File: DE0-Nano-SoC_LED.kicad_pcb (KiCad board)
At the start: 2 copper layers, 96 x 178.3 mm, 23 parts, among them J1 Conn_02x08_Odd_Even, J10 Conn_01x01, J11 Conn_01x01, J12 Conn_01x01, J13 Conn_01x01, J14 Conn_01x01, J15 Conn_01x01, J16 Conn_01x10, J17 Conn_01x08, J18 Conn_01x06, J19 Conn_01x08, J2 Conn_02x08_Odd_Even, J3 Conn_02x20_Odd_Even, J4 Conn_02x20_Odd_Even, J5 Conn_02x08_Odd_Even, J6 Conn_02x08_Odd_Even, J7 Conn_02x08_Odd_Even, J8 Conn_01x01, J9 Conn_01x01, U1 74HC245, U2 74HC245

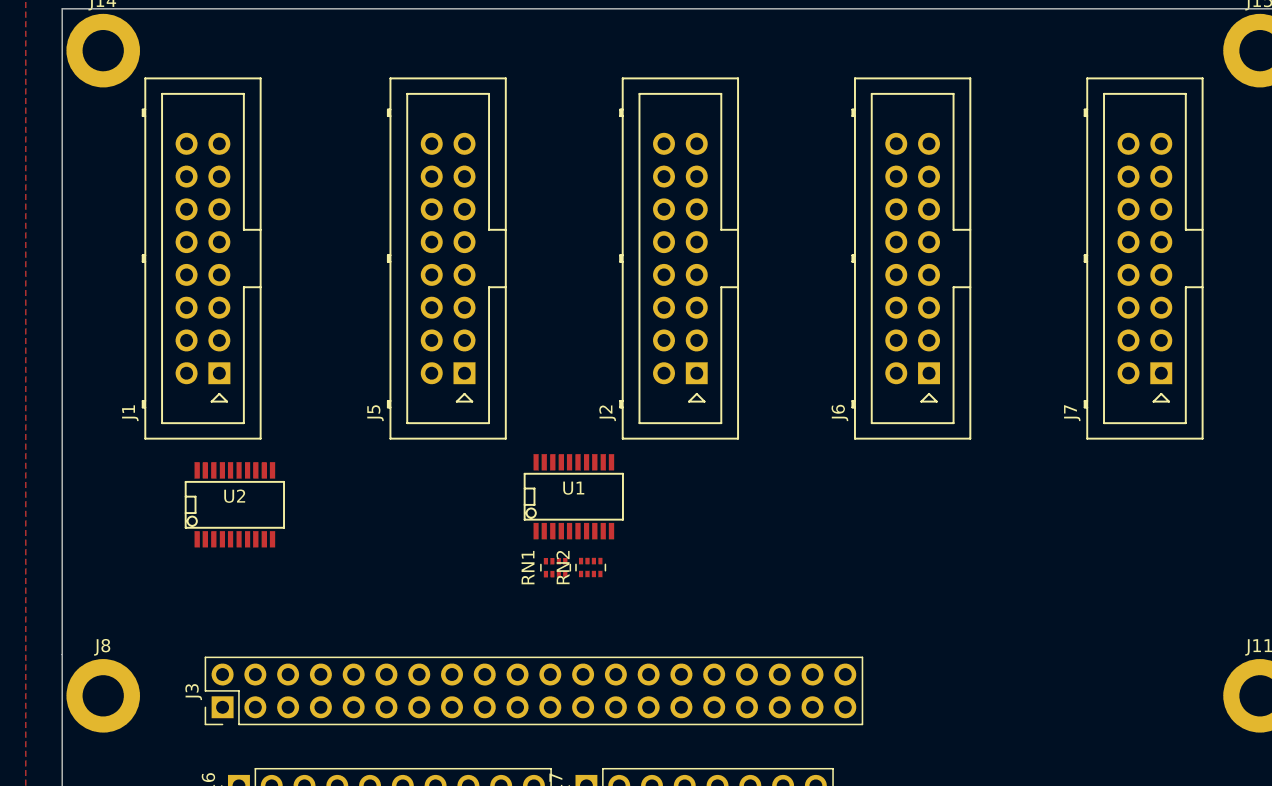
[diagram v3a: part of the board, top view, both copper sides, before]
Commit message: half of the components are almost placed
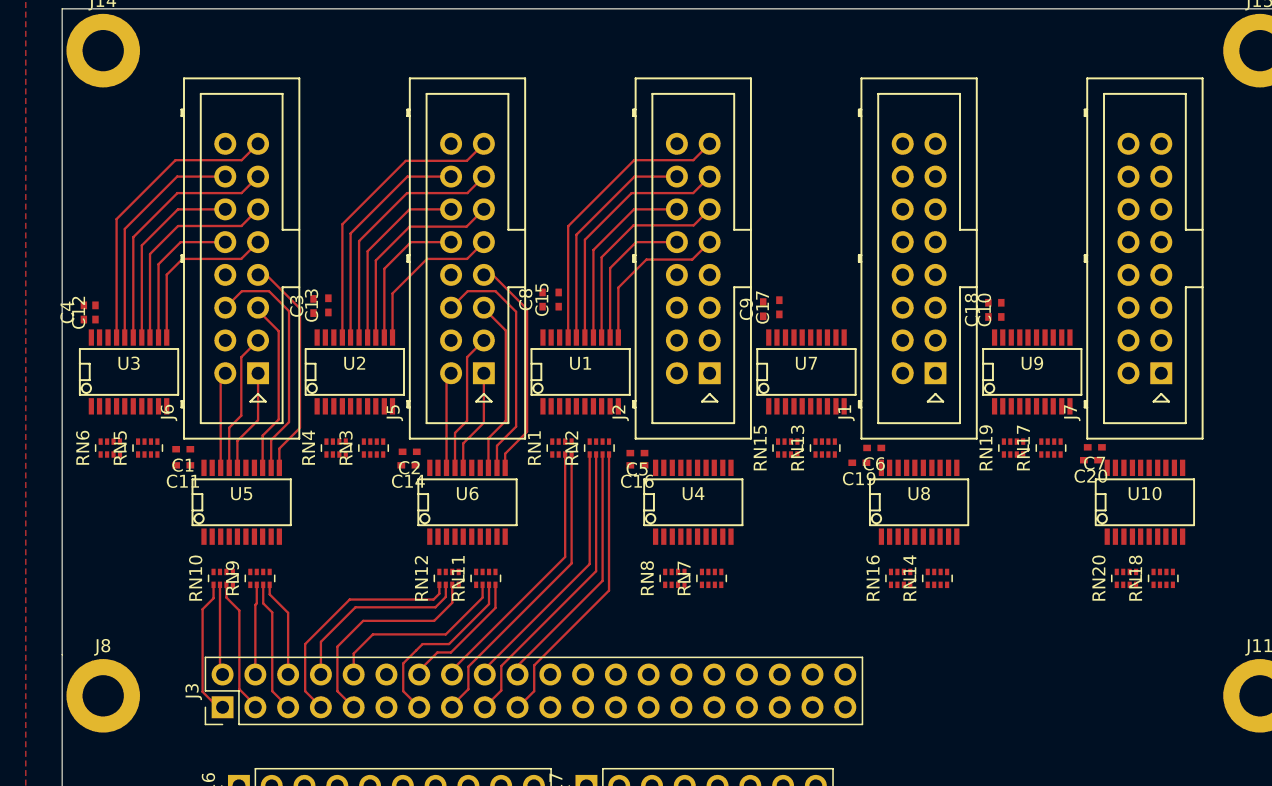
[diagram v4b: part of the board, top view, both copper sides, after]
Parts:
- added C1: 0.1, Capacitors_SMD:C_0402_NoSilk, F.Cu at (76.2, 50.9)
- added C10: 0.1, Capacitors_SMD:C_0402_NoSilk, F.Cu at (139.6, 40.1)
- added C11: 0.01, Capacitors_SMD:C_0402_NoSilk, F.Cu at (76.2, 52.1)
- added C12: 0.01, Capacitors_SMD:C_0402_NoSilk, F.Cu at (69.4, 40.3)
- added C13: 0.01, Capacitors_SMD:C_0402_NoSilk, F.Cu at (87.5, 39.7)
- added C14: 0.01, Capacitors_SMD:C_0402_NoSilk, F.Cu at (93.7, 52.1)
- added C15: 0.01, Capacitors_SMD:C_0402_NoSilk, F.Cu at (105.3, 39.3)
- added C16: 0.01, Capacitors_SMD:C_0402_NoSilk, F.Cu at (111.4, 52.1)
- added C17: 0.01, Capacitors_SMD:C_0402_NoSilk, F.Cu at (122.4, 39.9)
- added C18: 0.01, Capacitors_SMD:C_0402_NoSilk, F.Cu at (138.6, 40.1)
- added C19: 0.01, Capacitors_SMD:C_0402_NoSilk, F.Cu at (128.6, 51.9)
- added C2: 0.1, Capacitors_SMD:C_0402_NoSilk, F.Cu at (93.8, 51.1)
- added C20: 0.01, Capacitors_SMD:C_0402_NoSilk, F.Cu at (146.6, 51.7)
- added C3: 0.1, Capacitors_SMD:C_0402_NoSilk, F.Cu at (86.3, 39.8)
- added C4: 0.1, Capacitors_SMD:C_0402_NoSilk, F.Cu at (68.5, 40.3)
- added C5: 0.1, Capacitors_SMD:C_0402_NoSilk, F.Cu at (111.4, 51.2)
- added C6: 0.1, Capacitors_SMD:C_0402_NoSilk, F.Cu at (129.8, 50.8)
- added C7: 0.1, Capacitors_SMD:C_0402_NoSilk, F.Cu at (146.8, 50.7)
- added C8: 0.1, Capacitors_SMD:C_0402_NoSilk, F.Cu at (104.0, 39.3)
- added C9: 0.1, Capacitors_SMD:C_0402_NoSilk, F.Cu at (121.2, 40.0)
- added RN10: R_Pack04, Resistors_SMD:R_Array_Concave_4x0402, F.Cu at (79.3, 60.9)
- added RN11: R_Pack04, Resistors_SMD:R_Array_Concave_4x0402, F.Cu at (99.7, 60.9)
- added RN12: R_Pack04, Resistors_SMD:R_Array_Concave_4x0402, F.Cu at (96.8, 60.9)
- added RN13: R_Pack04, Resistors_SMD:R_Array_Concave_4x0402, F.Cu at (126.0, 50.8)
- added RN14: R_Pack04, Resistors_SMD:R_Array_Concave_4x0402, F.Cu at (134.7, 60.9)
- added RN15: R_Pack04, Resistors_SMD:R_Array_Concave_4x0402, F.Cu at (123.0, 50.8)
- added RN16: R_Pack04, Resistors_SMD:R_Array_Concave_4x0402, F.Cu at (131.8, 60.9)
- added RN17: R_Pack04, Resistors_SMD:R_Array_Concave_4x0402, F.Cu at (143.4, 50.8)
- added RN18: R_Pack04, Resistors_SMD:R_Array_Concave_4x0402, F.Cu at (152.2, 60.9)
- added RN19: R_Pack04, Resistors_SMD:R_Array_Concave_4x0402, F.Cu at (140.6, 50.8)
- added RN20: R_Pack04, Resistors_SMD:R_Array_Concave_4x0402, F.Cu at (149.3, 60.9)
- added RN3: R_Pack04, Resistors_SMD:R_Array_Concave_4x0402, F.Cu at (91.0, 50.8)
- added RN4: R_Pack04, Resistors_SMD:R_Array_Concave_4x0402, F.Cu at (88.0, 50.8)
- added RN5: R_Pack04, Resistors_SMD:R_Array_Concave_4x0402, F.Cu at (73.5, 50.8)
- added RN6: R_Pack04, Resistors_SMD:R_Array_Concave_4x0402, F.Cu at (70.5, 50.8)
- added RN7: R_Pack04, Resistors_SMD:R_Array_Concave_4x0402, F.Cu at (117.2, 60.9)
- added RN8: R_Pack04, Resistors_SMD:R_Array_Concave_4x0402, F.Cu at (114.3, 60.9)
- added RN9: R_Pack04, Resistors_SMD:R_Array_Concave_4x0402, F.Cu at (82.2, 60.9)
- added U10: 74HC245, SMD_Packages:SSOP-20, F.Cu at (150.7, 55.0)
- added U3: 74HC245, SMD_Packages:SSOP-20, F.Cu at (72.0, 44.9)
- added U4: 74HC245, SMD_Packages:SSOP-20, F.Cu at (115.7, 55.0)
- added U5: 74HC245, SMD_Packages:SSOP-20, F.Cu at (80.7, 55.0)
- added U6: 74HC245, SMD_Packages:SSOP-20, F.Cu at (98.2, 55.0)
- added U7: 74HC245, SMD_Packages:SSOP-20, F.Cu at (124.5, 44.9)
- added U8: 74HC245, SMD_Packages:SSOP-20, F.Cu at (133.2, 55.0)
- added U9: 74HC245, SMD_Packages:SSOP-20, F.Cu at (142.0, 44.9)
- moved J1 55.5 mm to (134.5, 45.0)
- moved J6 52.0 mm to (82.0, 45.0)
- moved U2 13.9 mm to (89.5, 44.9)
- moved U1 9.68 mm to (107.0, 44.9)
- moved RN2 9.28 mm to (108.5, 50.8)
- moved RN1 9.28 mm to (105.5, 50.8)
- moved J5 1.50 mm to (99.5, 45.0)
- moved J2 1.00 mm to (117.0, 45.0)
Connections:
- net Net-(J3-Pad26) renamed /B2_3
- J1 pad 1: Net-(J1-Pad1) -> /R1_4_1
- J1 pad 10: Net-(J1-Pad10) -> /B_4_1
- J1 pad 11: Net-(J1-Pad11) -> /C_4_1
- J1 pad 12: Net-(J1-Pad12) -> /D_4_1
- J1 pad 13: Net-(J1-Pad13) -> /CLK_4_1
- J1 pad 14: Net-(J1-Pad14) -> /LAT_4_1
- J1 pad 15: Net-(J1-Pad15) -> /OE_4_1
- J1 pad 2: Net-(J1-Pad2) -> /G1_4_1
- J1 pad 3: Net-(J1-Pad3) -> /B1_4_1
- J1 pad 5: Net-(J1-Pad5) -> /R2_4_1
- J1 pad 6: Net-(J1-Pad6) -> /G2_4_1
- J1 pad 7: Net-(J1-Pad7) -> /B2_4_1
- J1 pad 9: Net-(J1-Pad9) -> /A_4_1
- J16 pad 9: Net-(J16-Pad9) -> /OE__1
- J2 pad 1: Net-(J2-Pad1) -> /R1_3_1
- J2 pad 10: Net-(J2-Pad10) -> /B_3_1
- J2 pad 11: Net-(J2-Pad11) -> /C_3_1
- J2 pad 12: Net-(J2-Pad12) -> /D_3_1
- J2 pad 13: Net-(J2-Pad13) -> /CLK_3_1
- J2 pad 14: Net-(J2-Pad14) -> /LAT_3_1
- J2 pad 15: Net-(J2-Pad15) -> /OE_3_1
- J2 pad 2: Net-(J2-Pad2) -> /G1_3_1
- J2 pad 3: Net-(J2-Pad3) -> /B1_3_1
- J2 pad 5: Net-(J2-Pad5) -> /R2_3_1
- J2 pad 6: Net-(J2-Pad6) -> /G2_3_1
- J2 pad 7: Net-(J2-Pad7) -> /B2_3_1
- J2 pad 9: Net-(J2-Pad9) -> /A_3_1
- J3 pad 1: Net-(J3-Pad1) -> /G1_1
- J3 pad 10: Net-(J3-Pad10) -> /R2_2
- J3 pad 13: Net-(J3-Pad13) -> /G2_2
- J3 pad 14: Net-(J3-Pad14) -> /B2_2
- J3 pad 15: Net-(J3-Pad15) -> /CLK__1
- J3 pad 16: Net-(J3-Pad16) -> /LAT__1
- J3 pad 17: Net-(J3-Pad17) -> /C__1
- J3 pad 18: Net-(J3-Pad18) -> /D__1
- J3 pad 19: Net-(J3-Pad19) -> /A__1
- J3 pad 2: Net-(J3-Pad2) -> /B1_1
- J3 pad 20: Net-(J3-Pad20) -> /B__1
- J3 pad 21: Net-(J3-Pad21) -> /G1_3
- J3 pad 22: Net-(J3-Pad22) -> /B1_3
- J3 pad 23: Net-(J3-Pad23) -> /R1_3
- J3 pad 24: Net-(J3-Pad24) -> /R2_3
- J3 pad 25: Net-(J3-Pad25) -> /G2_3
- J3 pad 27: Net-(J3-Pad27) -> /G1_4
- J3 pad 28: Net-(J3-Pad28) -> /B1_4
- J3 pad 3: Net-(J3-Pad3) -> /R1_1
- J3 pad 31: Net-(J3-Pad31) -> /R1_4
- J3 pad 32: Net-(J3-Pad32) -> /R2_4
- J3 pad 33: Net-(J3-Pad33) -> /G2_4
- J3 pad 34: Net-(J3-Pad34) -> /B2_4
- J3 pad 35: Net-(J3-Pad35) -> /G1_5
- J3 pad 36: Net-(J3-Pad36) -> /B1_5
- J3 pad 37: Net-(J3-Pad37) -> /R1_5
- J3 pad 38: Net-(J3-Pad38) -> /R2_5
- J3 pad 39: Net-(J3-Pad39) -> /G2_5
- J3 pad 4: Net-(J3-Pad4) -> /R2_1
- J3 pad 40: Net-(J3-Pad40) -> /B2_5
- J3 pad 5: Net-(J3-Pad5) -> /G2_1
- J3 pad 6: Net-(J3-Pad6) -> /B2_1
- J3 pad 7: Net-(J3-Pad7) -> /G1_2
- J3 pad 8: Net-(J3-Pad8) -> /B1_2
- J3 pad 9: Net-(J3-Pad9) -> /R1_2
- J5 pad 1: Net-(J5-Pad1) -> /R1_2_1
- J5 pad 10: Net-(J5-Pad10) -> /B_2_1
- J5 pad 11: Net-(J5-Pad11) -> /C_2_1
- J5 pad 12: Net-(J5-Pad12) -> /D_2_1
- J5 pad 13: Net-(J5-Pad13) -> /CLK_2_1
- J5 pad 14: Net-(J5-Pad14) -> /LAT_2_1
- J5 pad 15: Net-(J5-Pad15) -> /OE_2_1
- J5 pad 2: Net-(J5-Pad2) -> /G1_2_1
- J5 pad 3: Net-(J5-Pad3) -> /B1_2_1
- J5 pad 5: Net-(J5-Pad5) -> /R2_2_1
- J5 pad 6: Net-(J5-Pad6) -> /G2_2_1
- J5 pad 7: Net-(J5-Pad7) -> /B2_2_1
- J5 pad 9: Net-(J5-Pad9) -> /A_2_1
- J6 pad 1: Net-(J6-Pad1) -> /R1_1_1
- J6 pad 10: Net-(J6-Pad10) -> /B_1_1
- J6 pad 11: Net-(J6-Pad11) -> /C_1_1
- J6 pad 12: Net-(J6-Pad12) -> /D_1_1
- J6 pad 13: Net-(J6-Pad13) -> /CLK_1_1
- J6 pad 14: Net-(J6-Pad14) -> /LAT_1_1
- J6 pad 15: Net-(J6-Pad15) -> /OE_1_1
- J6 pad 2: Net-(J6-Pad2) -> /G1_1_1
- J6 pad 3: Net-(J6-Pad3) -> /B1_1_1
- J6 pad 5: Net-(J6-Pad5) -> /R2_1_1
- J6 pad 6: Net-(J6-Pad6) -> /G2_1_1
- J6 pad 7: Net-(J6-Pad7) -> /B2_1_1
- J6 pad 9: Net-(J6-Pad9) -> /A_1_1
- J7 pad 1: Net-(J7-Pad1) -> /R1_5_1
- J7 pad 10: Net-(J7-Pad10) -> /B_5_1
- J7 pad 11: Net-(J7-Pad11) -> /C_5_1
- J7 pad 12: Net-(J7-Pad12) -> /D_5_1
- J7 pad 13: Net-(J7-Pad13) -> /CLK_5_1
- J7 pad 14: Net-(J7-Pad14) -> /LAT_5_1
- J7 pad 15: Net-(J7-Pad15) -> /OE_5_1
- J7 pad 2: Net-(J7-Pad2) -> /G1_5_1
- J7 pad 3: Net-(J7-Pad3) -> /B1_5_1
- J7 pad 5: Net-(J7-Pad5) -> /R2_5_1
- J7 pad 6: Net-(J7-Pad6) -> /G2_5_1
- J7 pad 7: Net-(J7-Pad7) -> /B2_5_1
- J7 pad 9: Net-(J7-Pad9) -> /A_5_1
- RN1 pad 2: Net-(RN1-Pad2) -> /OE__1
- RN1 pad 3: Net-(RN1-Pad3) -> /LAT__1
- RN1 pad 4: Net-(RN1-Pad4) -> /CLK__1
- RN2 pad 1: Net-(RN2-Pad1) -> /D__1
- RN2 pad 2: Net-(RN2-Pad2) -> /C__1
- RN2 pad 3: Net-(RN2-Pad3) -> /B__1
- RN2 pad 4: Net-(RN2-Pad4) -> /A__1
- U1 pad 11: Net-(U1-Pad11) -> /A_3_1
- U1 pad 12: Net-(U1-Pad12) -> /B_3_1
- U1 pad 13: Net-(U1-Pad13) -> /C_3_1
- U1 pad 14: Net-(U1-Pad14) -> /D_3_1
- U1 pad 15: Net-(U1-Pad15) -> /CLK_3_1
- U1 pad 16: Net-(U1-Pad16) -> /LAT_3_1
- U1 pad 17: Net-(U1-Pad17) -> /OE_3_1
- U1 pad 2: Net-(RN1-Pad8) -> GND
- U2 pad 11: Net-(U2-Pad11) -> /A_2_1
- U2 pad 12: Net-(U2-Pad12) -> /B_2_1
- U2 pad 13: Net-(U2-Pad13) -> /C_2_1
- U2 pad 14: Net-(U2-Pad14) -> /D_2_1
- U2 pad 15: Net-(U2-Pad15) -> /CLK_2_1
- U2 pad 16: Net-(U2-Pad16) -> /LAT_2_1
- U2 pad 17: Net-(U2-Pad17) -> /OE_2_1
- U2 pad 2: Net-(U2-Pad2) -> GND
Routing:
- net /CLK__1: track 0.00 -> 23.4 mm
- net /C__1: track 0.00 -> 23.2 mm
- net /OE_1_1: track 0.00 -> 22.6 mm
- net /A__1: track 0.00 -> 22.6 mm
- net /OE_2_1: track 0.00 -> 22.3 mm
- net /OE_3_1: track 0.00 -> 22.2 mm
- net /LAT__1: track 0.00 -> 20.7 mm
- net /D__1: track 0.00 -> 20.4 mm
- net /B__1: track 0.00 -> 19.8 mm
- net /CLK_1_1: track 0.00 -> 19.4 mm
- net /CLK_3_1: track 0.00 -> 19.3 mm
- net /CLK_2_1: track 0.00 -> 19.2 mm
- net /G2_2_1: track 0.00 -> 18.9 mm
- net /G2_1_1: track 0.00 -> 18.8 mm
- net /G1_2: track 0.00 -> 18.1 mm
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
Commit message: a lot of progress on pcb
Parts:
- moved RN10 0.50 mm to (79.3, 60.4)
- moved RN11 0.50 mm to (99.7, 60.4)
- moved RN12 0.50 mm to (96.8, 60.4)
- moved RN14 0.50 mm to (134.7, 60.4)
- moved RN16 0.50 mm to (131.8, 60.4)
- moved RN18 0.50 mm to (152.2, 60.4)
- moved RN20 0.50 mm to (149.3, 60.4)
- moved RN7 0.50 mm to (117.2, 60.4)
- moved RN8 0.50 mm to (114.3, 60.4)
- moved RN9 0.50 mm to (82.2, 60.4)
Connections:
- J3 pad 21: /G1_3 -> /B1_3
- J3 pad 22: /B1_3 -> /G1_3
- J3 pad 23: /R1_3 -> /R2_3
- J3 pad 24: /R2_3 -> /R1_3
- J3 pad 25: /G2_3 -> /B2_3
- J3 pad 26: /B2_3 -> /G2_3
- J3 pad 27: /G1_4 -> /B1_4
- J3 pad 28: /B1_4 -> /G1_4
- J3 pad 31: /R1_4 -> /R2_4
- J3 pad 32: /R2_4 -> /R1_4
- J3 pad 33: /G2_4 -> /B2_4
- J3 pad 34: /B2_4 -> /G2_4
- J3 pad 35: /G1_5 -> /B1_5
- J3 pad 36: /B1_5 -> /G1_5
- J3 pad 37: /R1_5 -> /G2_5
- J3 pad 38: /R2_5 -> /R1_5
- J3 pad 39: /G2_5 -> /B2_5
- J3 pad 40: /B2_5 -> /R2_5
- RN7 pad 4: /R2_3 -> /B2_3
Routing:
- net /D__1: track 20.4 -> 105.8 mm, vias 0 -> 3
- net /A__1: track 22.6 -> 99.1 mm, vias 0 -> 3
- net /B__1: track 19.8 -> 89.4 mm, vias 0 -> 2
- net /C__1: track 23.2 -> 92.5 mm, vias 0 -> 2
- net /CLK__1: track 23.4 -> 69.7 mm, vias 0 -> 2
- net /LAT__1: track 20.7 -> 64.3 mm, vias 0 -> 2
- net /B1_5: track 0.00 -> 32.7 mm
- net /G2_5: track 0.00 -> 32.4 mm
- net /B2_5: track 0.00 -> 31.0 mm
- net /G1_5: track 0.00 -> 30.2 mm
- net /R1_5: track 0.00 -> 28.4 mm
- net /R2_5: track 0.00 -> 28.1 mm
- net /B1_4: track 0.00 -> 24.8 mm
- net /R2_4: track 0.00 -> 22.8 mm
- net /G1_4: track 0.00 -> 22.5 mm
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
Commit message: more progress on pcb
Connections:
- J16 pad 7: Net-(J16-Pad7) -> /OE__1
- J16 pad 9: /OE__1 -> Net-(J16-Pad9)
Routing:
- net /OE__1: track 0.00 -> 116.8 mm, vias 0 -> 6
- net /CLK__1: track 69.7 -> 112.8 mm, vias 2 -> 5
- net /LAT__1: track 64.3 -> 106.2 mm, vias 2 -> 5
- net /B2_3: track 0.00 -> 14.1 mm
- net /C__1: track 92.5 -> 95.1 mm, vias 2 -> 4
- net /D__1: track 105.8 -> 108.2 mm, vias 3 -> 5
- net /B__1: track 89.4 -> 90.7 mm, vias 2 -> 4
- net /R1_5: track 28.4 -> 29.5 mm
- net /R2_4: track 22.8 -> 23.6 mm
- net /R1_4: track 18.5 -> 17.7 mm
- net /A__1: track 99.1 -> 98.4 mm, vias 3 -> 4
- net /B1_5: track 32.7 -> 33.3 mm
- net /B2_4: track 21.8 -> 22.3 mm

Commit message: pcb is almost done
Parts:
- moved C15 1.33 mm to (104.4, 40.3)
- moved C8 1.14 mm to (103.5, 40.3)
- moved C6 1.06 mm to (128.8, 51.3)
- moved C13 0.78 mm to (86.9, 40.3)
- moved C7 0.73 mm to (146.4, 51.3)
- moved C20 0.63 mm to (146.4, 52.3)
- moved C3 0.61 mm to (86.0, 40.3)
- moved C17 0.60 mm to (122.0, 40.3)
- moved C19 0.45 mm to (128.8, 52.3)
- moved C1 0.35 mm to (76.2, 51.2)
- moved C10 0.27 mm to (139.4, 40.3)
- moved C9 0.27 mm to (121.0, 40.3)
- moved C18 0.24 mm to (138.5, 40.3)
- moved C2 0.22 mm to (93.8, 51.3)
- moved C14 0.20 mm to (93.8, 52.3)
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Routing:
- net GND: track 0.00 -> 135.7 mm, vias 0 -> 98
- net VCC: track 0.00 -> 56.1 mm, vias 0 -> 38
- net /C__1: track 95.1 -> 119.0 mm, vias 4 -> 5
- net /B__1: track 90.7 -> 113.2 mm, vias 4 -> 5
- net /A__1: track 98.4 -> 119.5 mm, vias 4 -> 5
- net /OE__1: track 116.8 -> 118.7 mm
- net /LAT__1: track 106.2 -> 107.7 mm
- net /D__1: track 108.2 -> 109.6 mm
- net /CLK__1: track 112.8 -> 114.0 mm
- net /R1_4: track 17.7 -> 18.7 mm
- net /A_5_1: track 12.0 -> 12.9 mm
- net /A_2_1: track 12.1 -> 12.9 mm
- net /A_4_1: track 12.2 -> 12.9 mm
- added copper zone on B.Cu, net GND
- added copper zone on B.Cu, net VCC
- added copper zone on F.Cu, net VCC
